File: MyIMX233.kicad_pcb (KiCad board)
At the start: 2 copper layers, 74.1 x 92 mm, 69 parts, among them IC1 iMX233, IC2 DDR_SDRAM_MT46_x16, J1 USB_A, J2 Micro_SD_Card, P1 P4v2, P2 1v2, P3 VDDA1v8, P4 2v5, P5 3v3, SW1 SWITCH_PUSHBUTTON, Y1 24Mhz

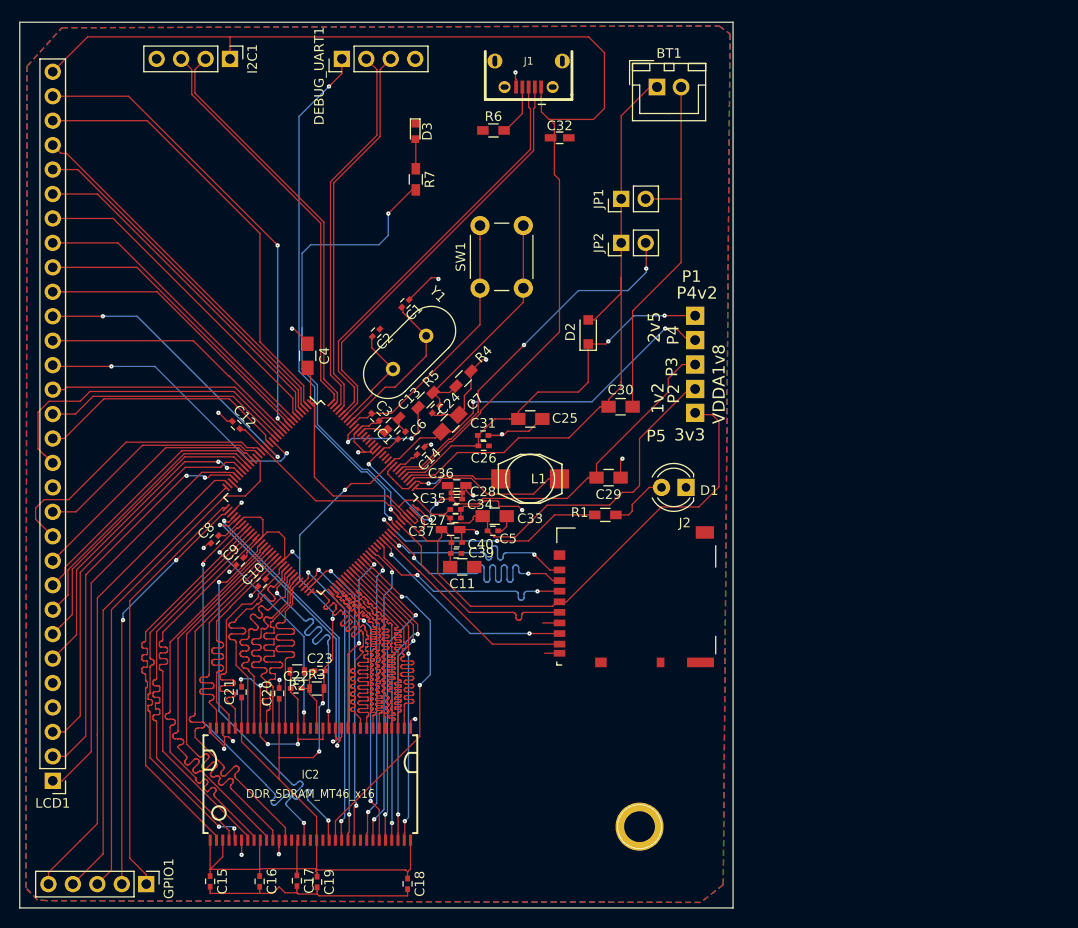
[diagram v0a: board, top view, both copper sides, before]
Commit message: updated via size
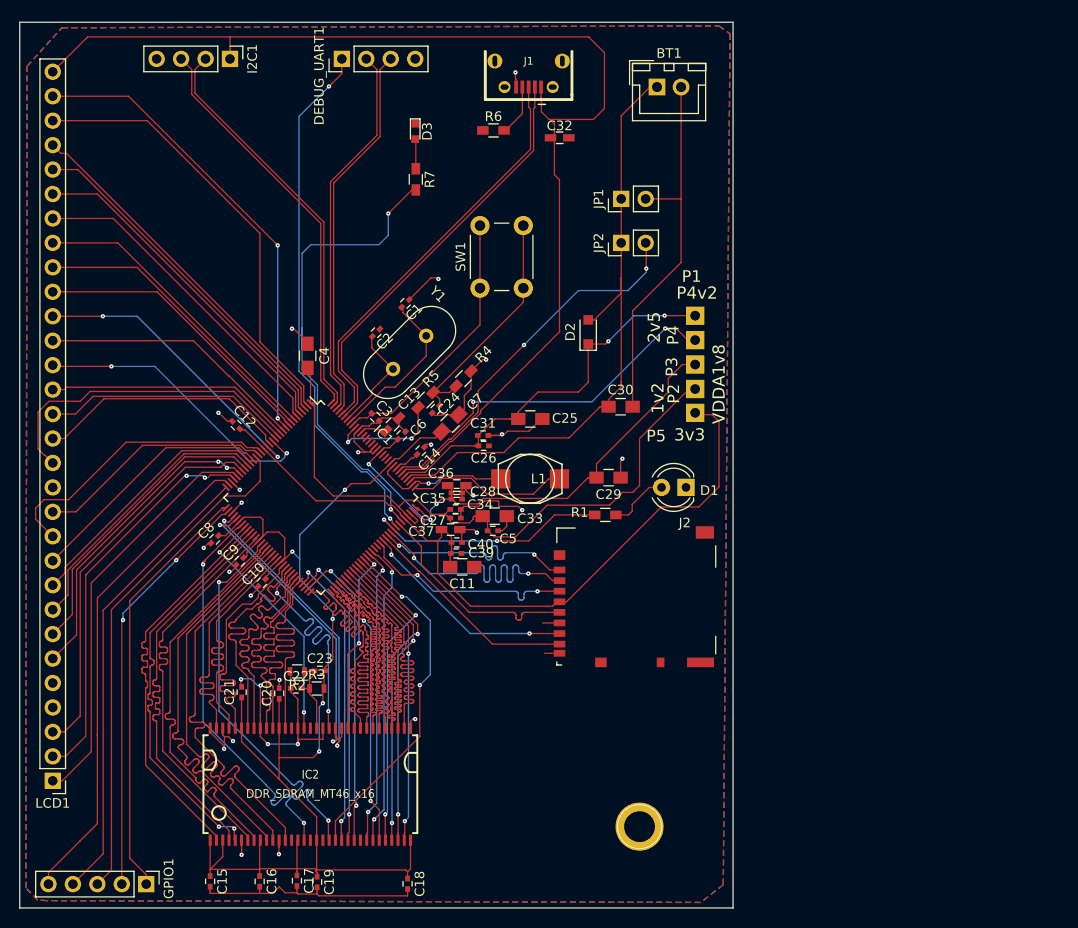
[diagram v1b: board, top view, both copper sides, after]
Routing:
- net GND: track 177.3 -> 176.7 mm
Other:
- net class Default: via_drill 0.1 -> 0.15
- rule via_min_drill: 0.1 -> 0.15

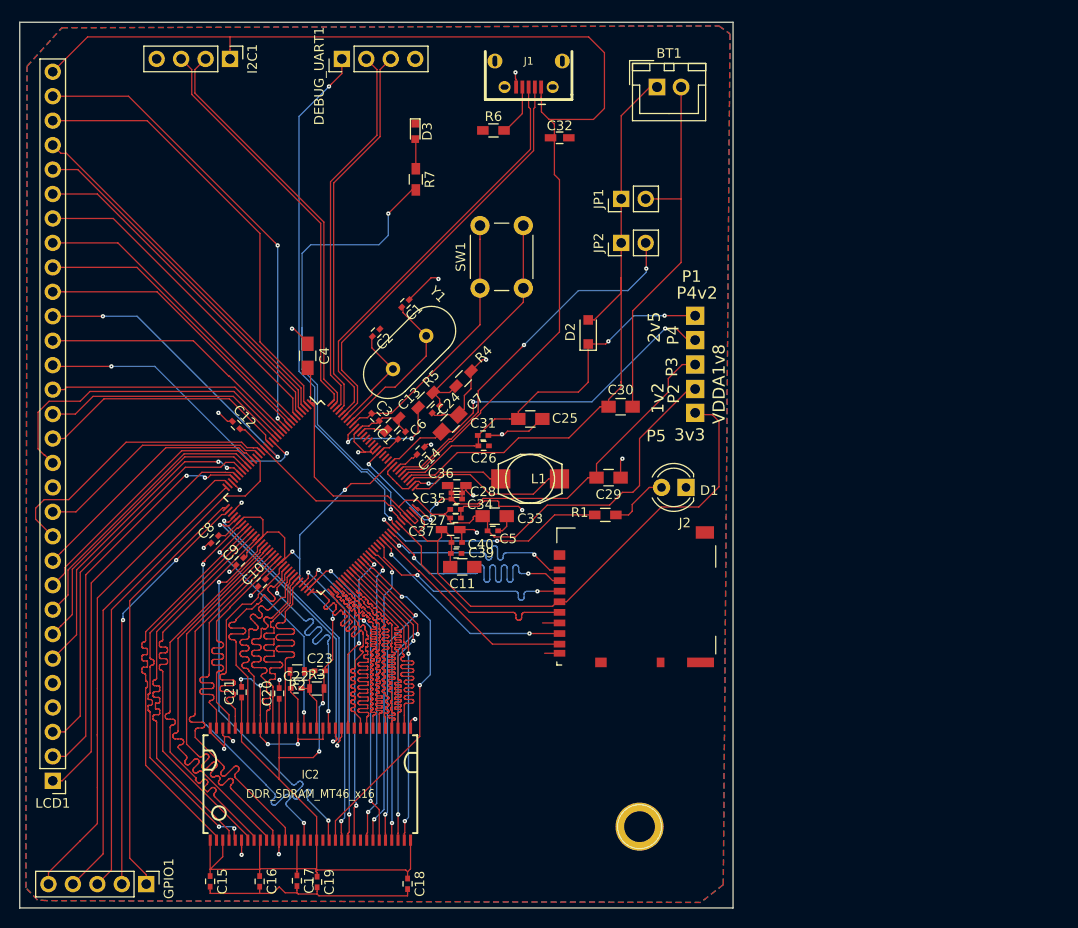
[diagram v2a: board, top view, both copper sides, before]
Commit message: new uSD card connector added
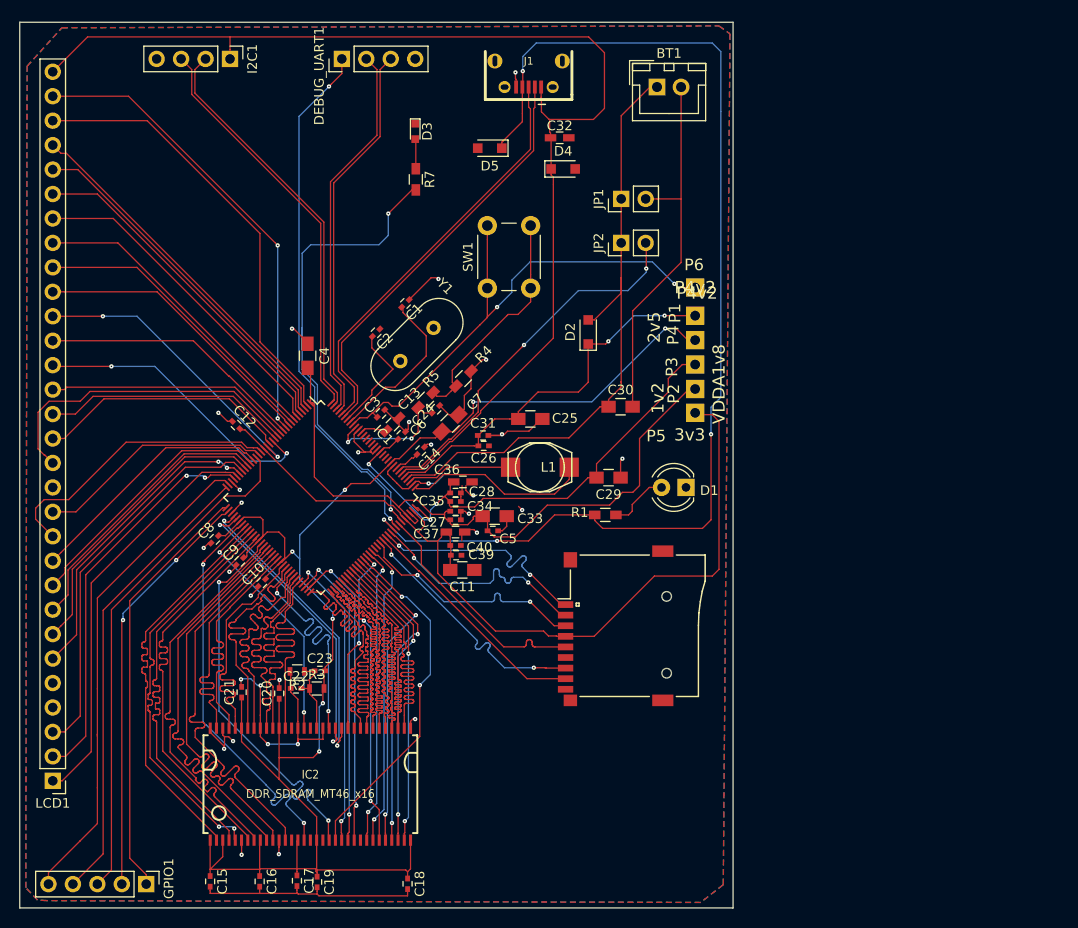
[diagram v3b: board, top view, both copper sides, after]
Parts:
- removed J2: Micro_SD_Card, mylib:microSD_Card_Receptacle_Hirose_DM3AT-SF-PEJM5
- removed R6: 10k, Resistors_SMD:R_0603_HandSoldering
- removed REF**: 1pin, Connectors:1pin
- added D4: 5.1v, Diodes_SMD:D_SOD-323_HandSoldering, F.Cu at (122.2, 64.8)
- added D5: 5.1v, Diodes_SMD:D_SOD-323_HandSoldering, F.Cu at (114.6, 62.6)
- added P6: P4v2, iMX233-OLinuXino-NANO_Rev_BEagle:GOGO_TESTPAD2, F.Cu at (135.9, 77.1)
- added XS1: SD_ebay-uSD-push/push_SMD, mylib:uSDcard, F.Cu at (132.9, 112.2)
- J1: value USB_A -> USB_OTG; footprint conn-fci:CONN-10118194-0001LF-FCI -> mylib:CONN-10118194-0001LF-FCI
- R2, R3: value R -> 1K1%
- moved L1 1.58 mm to (119.8, 95.8)
- moved Y1 1.12 mm to (108.7, 81.3)
- moved SW1 0.76 mm to (114.3, 77.2)
- moved C36 0.74 mm to (111.8, 97.3)
- moved C3 0.69 mm to (103.3, 90.2), turned to 45 degrees
- moved C37 0.57 mm to (111.0, 102.5)
- moved C40 0.34 mm to (111.0, 103.9)
- moved C11 0.32 mm to (111.7, 106.4)
- moved C35 0.28 mm to (111.0, 99.3)
- moved C27 0.19 mm to (111.0, 101.2)
- moved C34 0.19 mm to (111.0, 100.3)
- moved C39 0.19 mm to (111.1, 104.9)
- moved C28 0.13 mm to (111.0, 98.4)
- turned C24 to 225 degrees
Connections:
- net Net-(IC1-Pad14) renamed /LCD_RS
- IC1 pad 119: Net-(IC1-Pad119) -> Net-(C24-Pad2)
- IC1 pad 88: Net-(IC1-Pad88) -> USB_ID
- J1 pad 4: Net-(J1-Pad4) -> USB_ID
- R1 pad 1: Net-(IC1-Pad88) -> USB_ID
- R4 pad 1: Net-(C24-Pad2) -> Net-(R4-Pad1)
- R5 pad 1: Net-(C24-Pad2) -> Net-(R4-Pad1)
- R5 pad 2: Net-(IC1-Pad119) -> Net-(C24-Pad2)
- SW1 pad 2: Net-(C24-Pad2) -> Net-(R4-Pad1)
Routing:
- net USB_ID: track 0.00 -> 119.7 mm, vias 0 -> 4
- net VDDXTAL_SYS: track 27.8 -> 55.0 mm, vias 0 -> 2
- net Net-(IC1-Pad88): track 25.4 -> 0.00 mm, vias 2 -> 0
- net Net-(R4-Pad1): track 0.00 -> 23.8 mm
- net Net-(IC1-Pad119): track 12.1 -> 0.00 mm, vias 2 -> 0
- net Net-(C24-Pad2): track 25.5 -> 13.8 mm, vias 0 -> 2
- net GND: track 176.7 -> 165.0 mm, vias 28 -> 30
- net 3v3_SYS: track 82.9 -> 90.7 mm
- net /SD3: track 30.5 -> 24.7 mm
- net Net-(J1-Pad4): track 5.38 -> 0.00 mm
- net /SD0: track 22.7 -> 26.8 mm
- net Net-(IC1-Pad97): track 17.1 -> 19.4 mm
- net /SD1: track 22.7 -> 24.8 mm
- net /SD_CMD: track 22.7 -> 24.7 mm
- net /SD_CLK: track 22.7 -> 24.7 mm
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
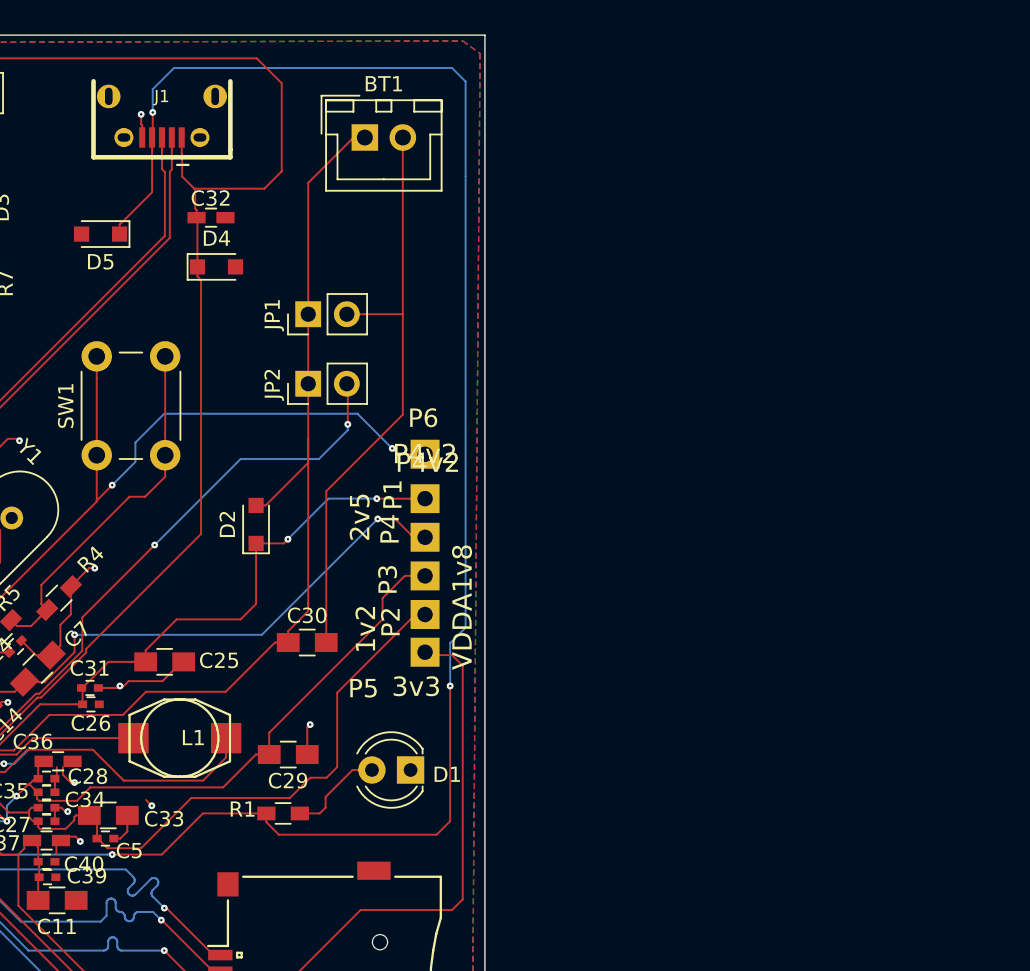
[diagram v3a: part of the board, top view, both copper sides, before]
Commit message: usb footprint updated
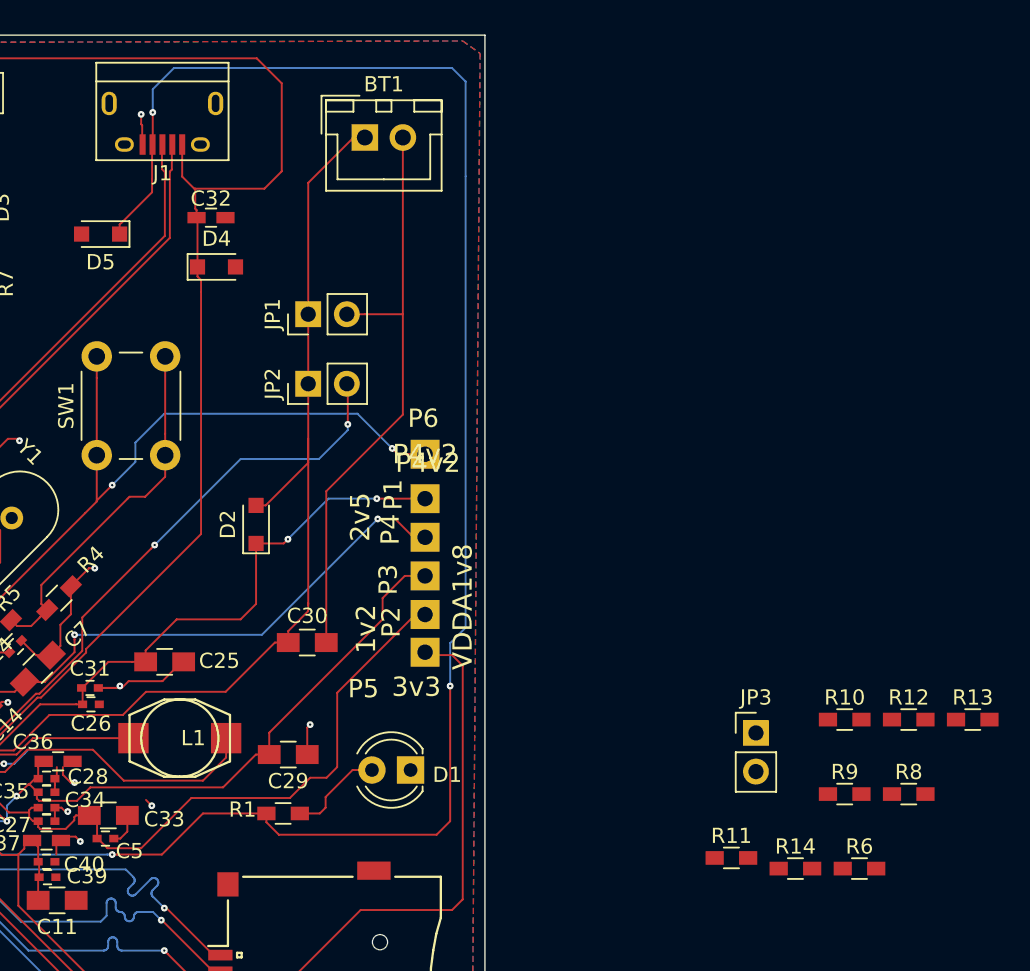
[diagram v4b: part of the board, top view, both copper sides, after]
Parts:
- added JP3: USB_boot, Pin_Headers:Pin_Header_Straight_1x02_Pitch2.54mm, F.Cu at (157.6, 95.4)
- added R10: 47k, Resistors_SMD:R_0603_HandSoldering, F.Cu at (163.5, 94.5)
- added R11: 47k, Resistors_SMD:R_0603_HandSoldering, F.Cu at (156.0, 103.6)
- added R12: 47k, Resistors_SMD:R_0603_HandSoldering, F.Cu at (167.7, 94.5)
- added R13: 47k, Resistors_SMD:R_0603_HandSoldering, F.Cu at (171.9, 94.5)
- added R14: 47k, Resistors_SMD:R_0603_HandSoldering, F.Cu at (160.2, 104.3)
- added R6: 4.7k, Resistors_SMD:R_0603_HandSoldering, F.Cu at (164.5, 104.3)
- added R8: 4.7k, Resistors_SMD:R_0603_HandSoldering, F.Cu at (167.7, 99.4)
- added R9: 47k, Resistors_SMD:R_0603_HandSoldering, F.Cu at (163.5, 99.4)
- J1: footprint mylib:CONN-10118194-0001LF-FCI -> mylib:USB_Micro-B_MOLEX_105017-0001
- moved J1 1.81 mm to (118.6, 55.4)
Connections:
- net Net-(IC1-Pad2) renamed /LCD0
- net Net-(IC1-Pad3) renamed /LCD1
- net Net-(IC1-Pad4) renamed /LCD2
- net Net-(IC1-Pad5) renamed /LCD3
- net Net-(IC1-Pad6) renamed /LCD4
- net Net-(IC1-Pad7) renamed /LCD5
- J1 pad 5: GND -> Net-(J1-Pad5)
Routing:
- net Net-(J1-Pad5): track 0.00 -> 1.55 mm, vias 0 -> 1
- net GND: track 165.0 -> 163.4 mm, vias 30 -> 29

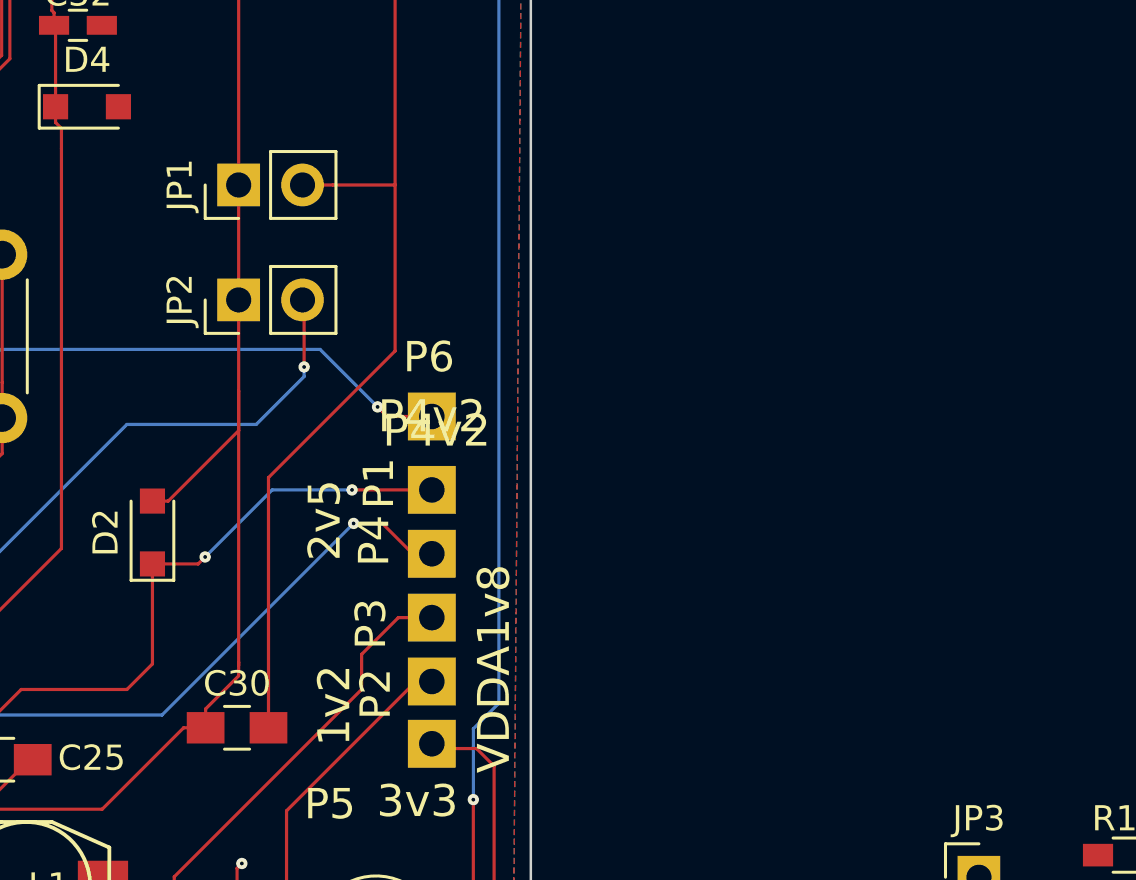
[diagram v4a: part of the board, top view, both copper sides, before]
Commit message: added boot resistors and 2.5v_VDDM is separated for ram, new battery connections with resistors for non battery mode
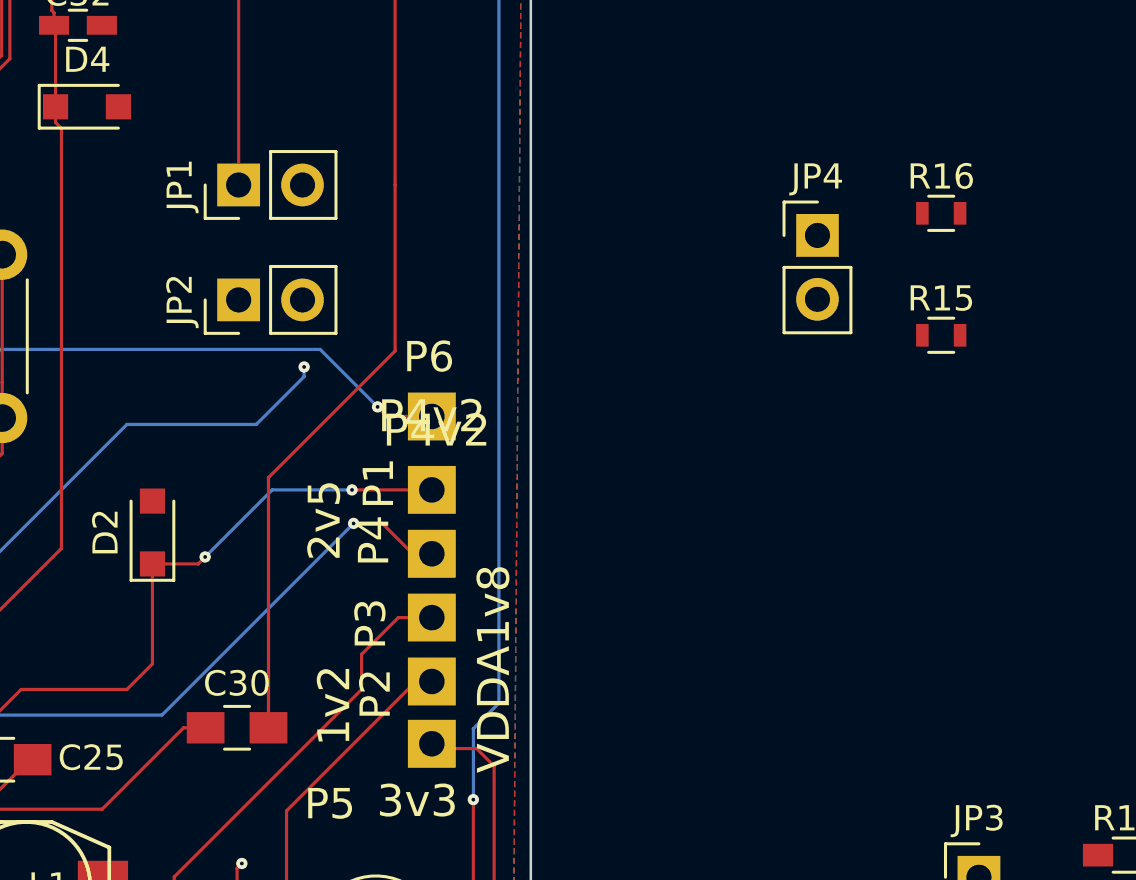
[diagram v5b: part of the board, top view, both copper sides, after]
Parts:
- added JP4: WithBatt, Pin_Headers:Pin_Header_Straight_1x02_Pitch2.54mm, F.Cu at (151.2, 69.9)
- added R15: 1K, Resistors_SMD:R_0603, F.Cu at (156.1, 73.9)
- added R16: 1K, Resistors_SMD:R_0603, F.Cu at (156.1, 69.0)
- D2: value D_Schottky -> D_Batt
- JP2: value Jumper -> WithoutBatt
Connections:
- C15 pad 1: 2V5_SYS -> 2V5_VDDM
- C16 pad 1: 2V5_SYS -> 2V5_VDDM
- C17 pad 1: 2V5_SYS -> 2V5_VDDM
- C18 pad 1: 2V5_SYS -> 2V5_VDDM
- C19 pad 1: 2V5_SYS -> 2V5_VDDM
- C20 pad 1: 2V5_SYS -> 2V5_VDDM
- C21 pad 1: 2V5_SYS -> 2V5_VDDM
- C23 pad 2: 2V5_SYS -> 2V5_VDDM
- C30 pad 2: GND -> Net-(C30-Pad2)
- IC1 pad 100: /+VE -> Net-(IC1-Pad100)
- IC1 pad 103: Net-(IC1-Pad103) -> /+VE
- IC2 pad 1: 2V5_SYS -> 2V5_VDDM
- IC2 pad 15: 2V5_SYS -> 2V5_VDDM
- IC2 pad 18: 2V5_SYS -> 2V5_VDDM
- IC2 pad 3: 2V5_SYS -> 2V5_VDDM
- IC2 pad 33: 2V5_SYS -> 2V5_VDDM
- IC2 pad 55: 2V5_SYS -> 2V5_VDDM
- IC2 pad 61: 2V5_SYS -> 2V5_VDDM
- IC2 pad 9: 2V5_SYS -> 2V5_VDDM
- J1 pad 5: Net-(J1-Pad5) -> GND
- JP1 pad 1: /+VE -> 2V5_SYS
- JP1 pad 2: GND -> 2V5_VDDM
- JP2 pad 1: /+VE -> Net-(C25-Pad2)
- JP2 pad 2: Net-(IC1-Pad103) -> Net-(JP2-Pad2)
- R3 pad 2: 2V5_SYS -> 2V5_VDDM
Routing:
- net Net-(IC1-Pad103): track 38.6 -> 0.00 mm, vias 2 -> 0
- net /+VE: track 66.1 -> 73.5 mm, vias 0 -> 2
- net GND: track 163.4 -> 161.3 mm, vias 29 -> 30
- net Net-(J1-Pad5): track 1.55 -> 0.00 mm, vias 1 -> 0
